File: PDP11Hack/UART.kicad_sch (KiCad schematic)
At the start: 14 parts, among them J1 Conn_01x02_Pin, J2 DB25_Receptacle, U1 HD-6402, U12 74LS00, U16 MAX232, U3 74LS02, U4 74LS126, U9 74LS139

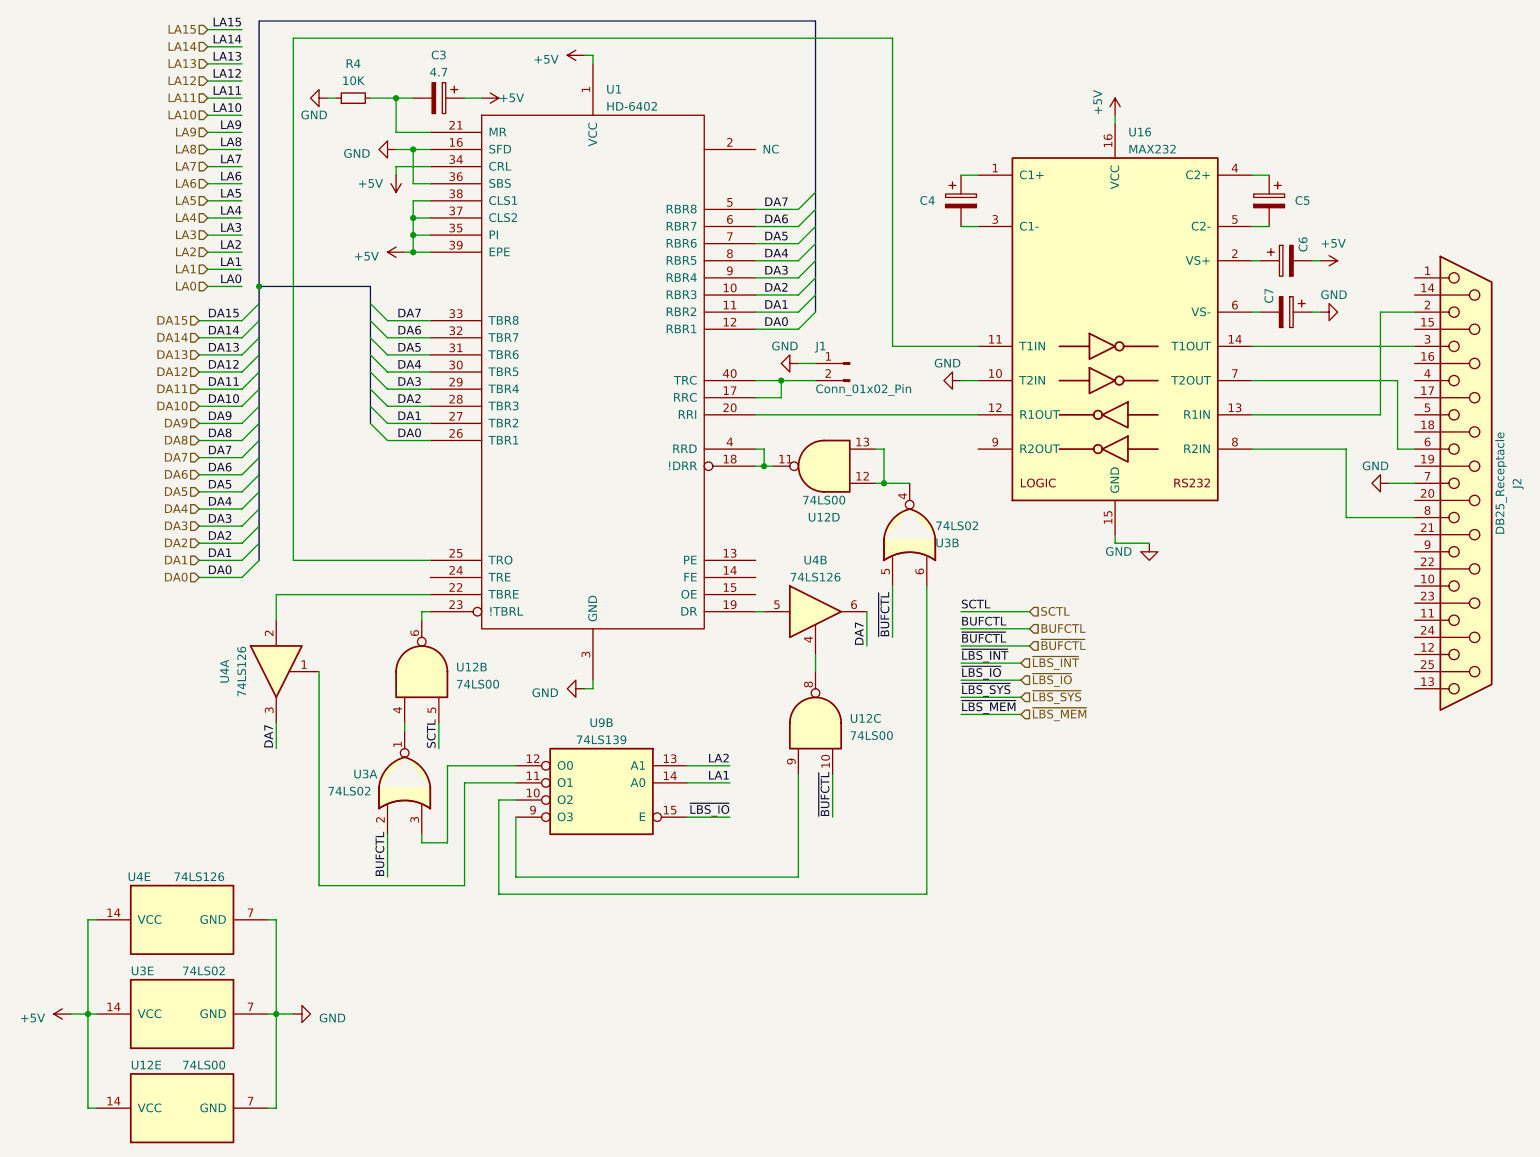
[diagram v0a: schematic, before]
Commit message: Assigned footprints.
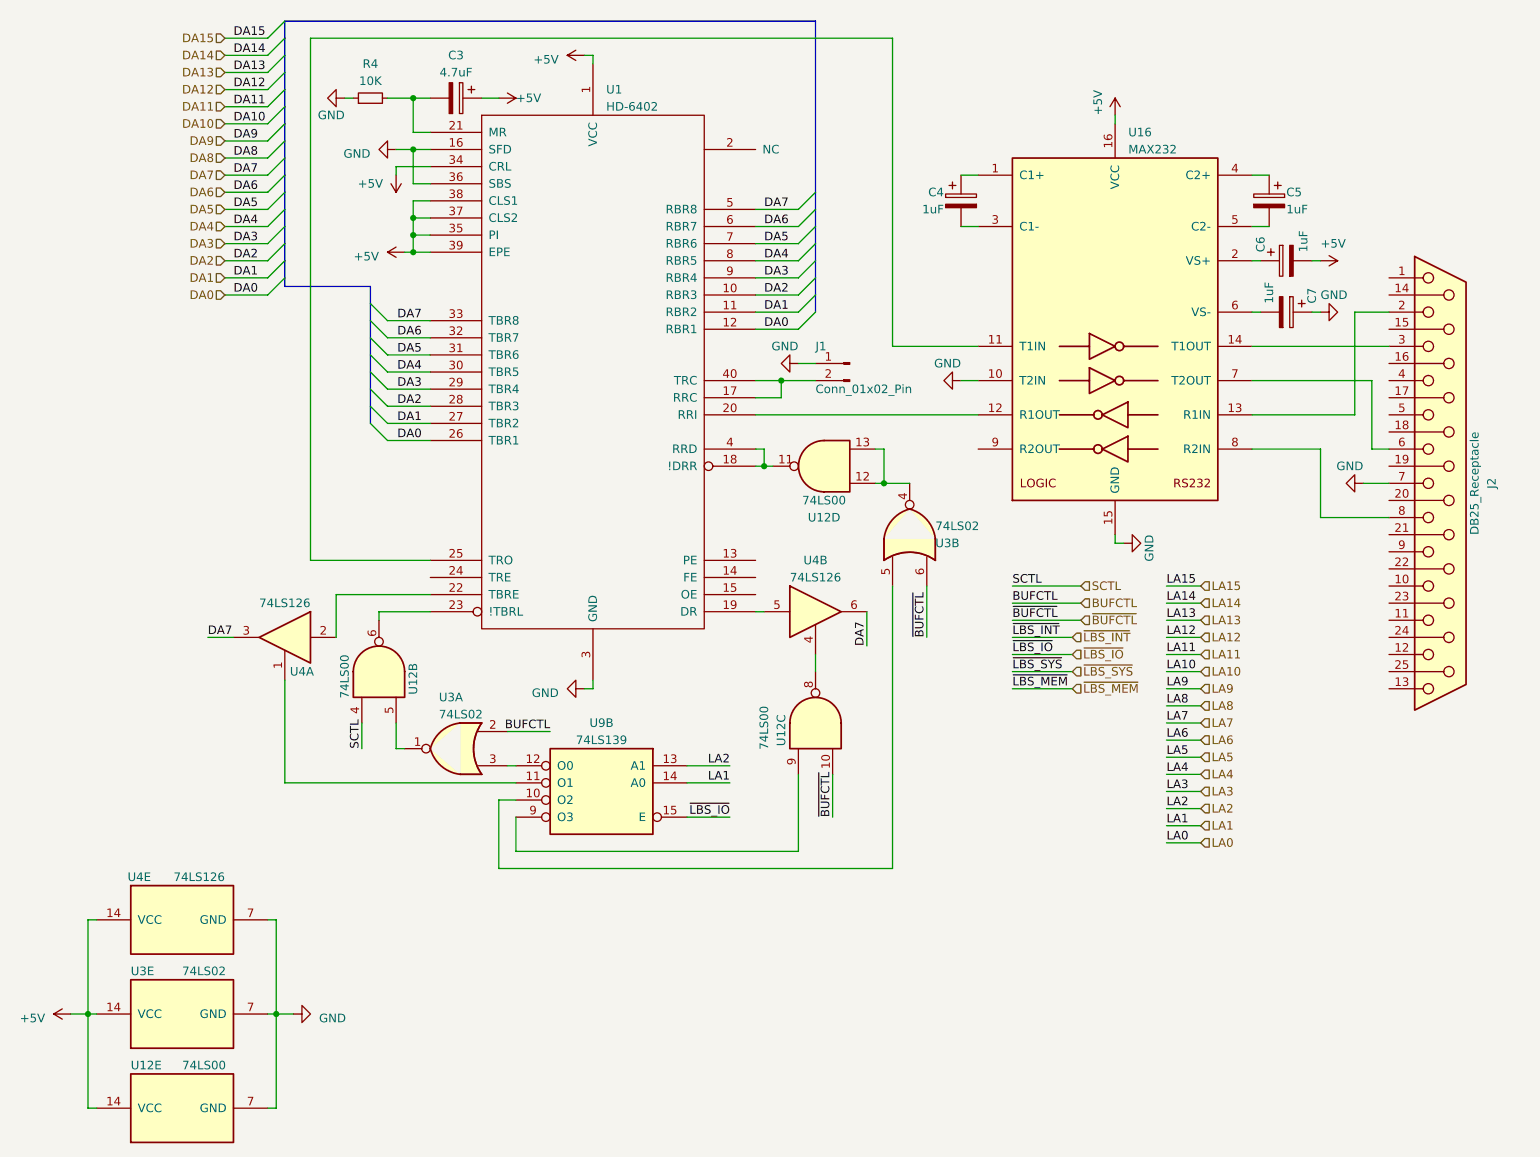
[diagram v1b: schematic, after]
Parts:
- C3: value 4.7 -> 4.7uF; footprint (none) -> Capacitor_THT:CP_Radial_D5.0mm_P2.00mm
- C4, C5, C6, C7: value ~ -> 1uF; footprint (none) -> Capacitor_THT:CP_Radial_D5.0mm_P2.00mm
- J1: footprint (none) -> Connector_PinHeader_1.27mm:PinHeader_1x02_P1.27mm_Vertical
- J2: footprint (none) -> SnapEDA Library:AMPHENOL_DB25S564TLF
- R4: footprint (none) -> Resistor_THT:R_Axial_DIN0207_L6.3mm_D2.5mm_P7.62mm_Horizontal
- U1: footprint MODULE -> Package_DIP:DIP-40_W15.24mm
- U12, U3, U4: footprint (none) -> Package_DIP:DIP-14_W7.62mm
- U16, U9: footprint (none) -> Package_DIP:DIP-16_W7.62mm
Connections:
- net SCTL: now also U12.4; no longer U12.5
- net ~{BUFCTL}: now also U3.6; no longer U3.5
- net at U3.1: now also U12.5; no longer U12.4
- net at U9.10 (O2): now also U3.5; no longer U3.6
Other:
- moved on the sheet: C3, J2, R4, U12B, U3A, U4A
